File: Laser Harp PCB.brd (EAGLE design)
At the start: 78.7 x 76.3 mm, 35 parts, among them J1 DCJ0202, X1 22-23-2021, X10 22-23-2051, X11 22-23-2021, X12 22-23-2021, X2 22-23-2021, X3 22-23-2021, X4 22-23-2021, X5 22-23-2021, X6 22-23-2021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

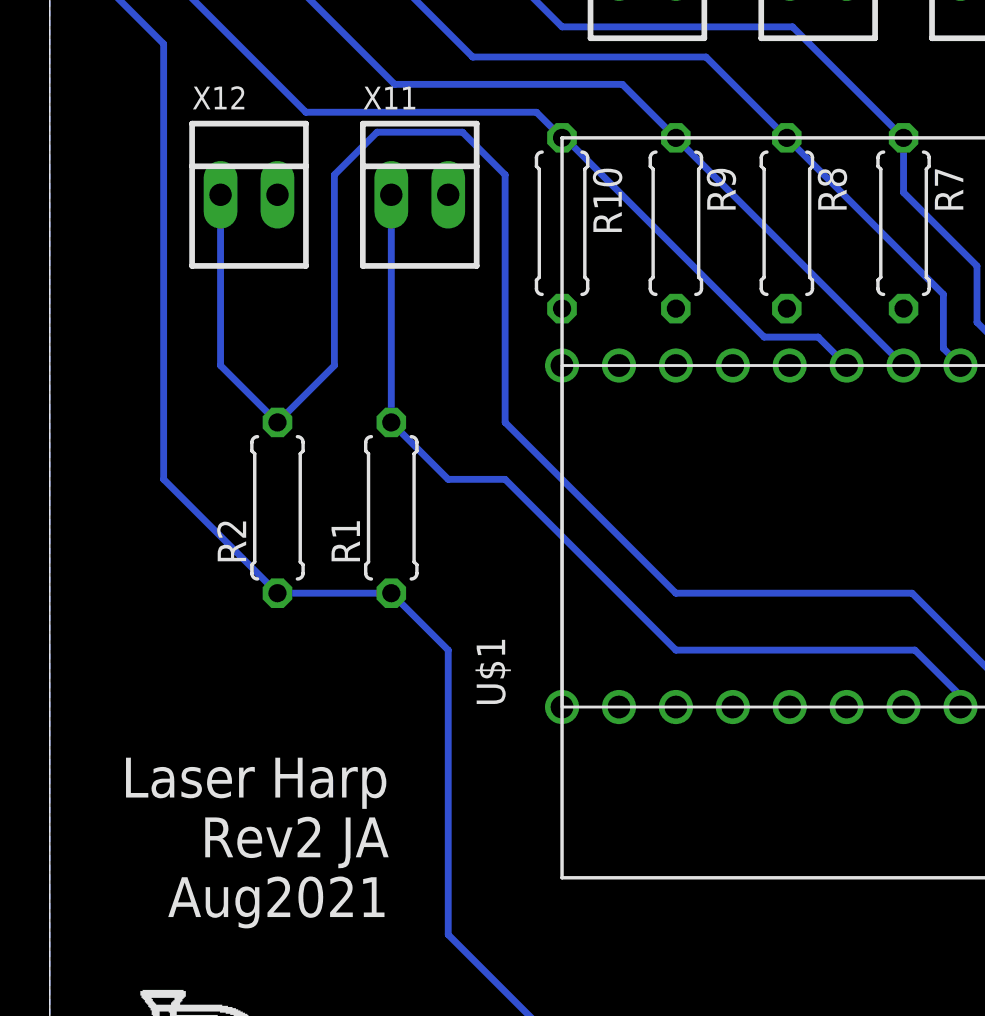
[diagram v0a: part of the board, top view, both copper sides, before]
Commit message: Update pin connections
The BJTs used to connect to pins 0 through 7 of the Teensy, but the Audio Shield uses pin 7 to transmit information from the micro sd card to the Teensy. I changed the connection from pin 7 to pin 8.
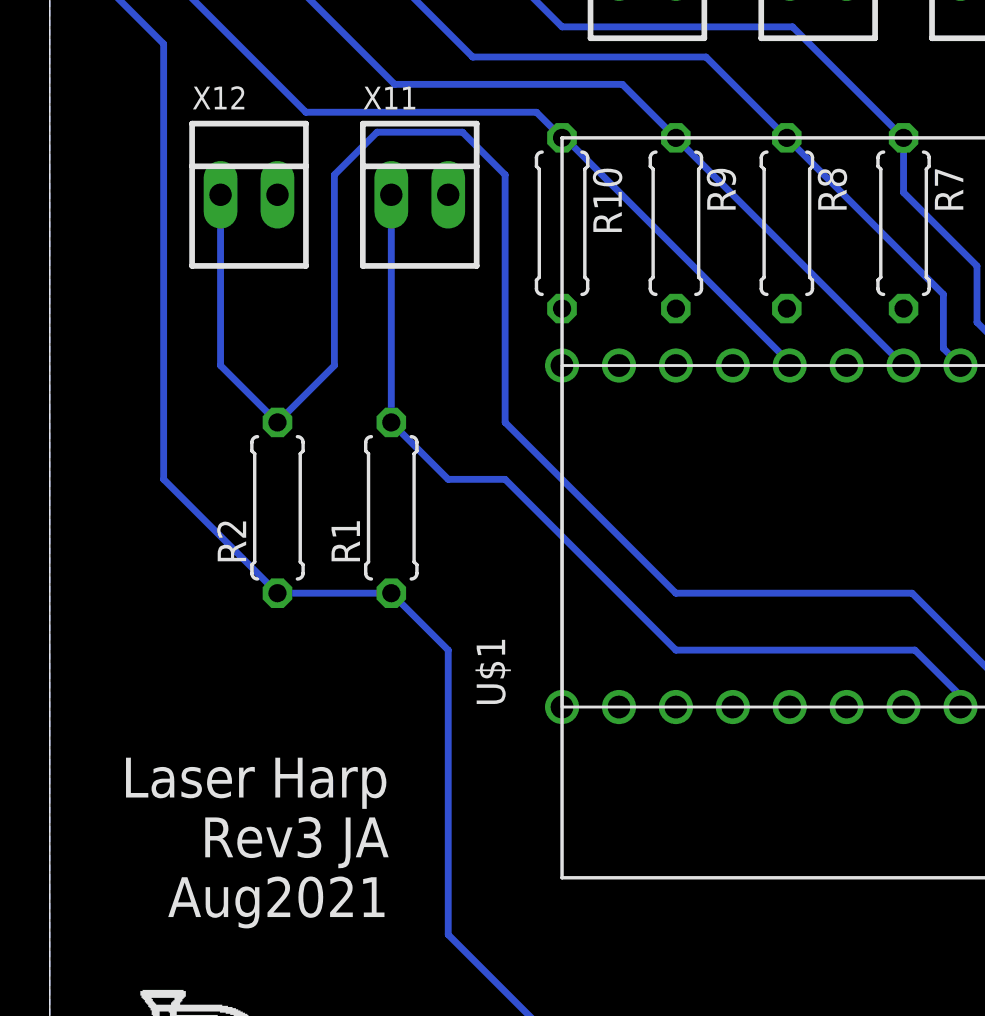
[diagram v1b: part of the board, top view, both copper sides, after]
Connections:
- net N$24: now also U$1.P$19; no longer U$1.P$20
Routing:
- net N$24: track 37.8 -> 35.3 mm
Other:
- board text added: "Laser Harp Rev3 JA Aug2021"
- board text removed: "Laser Harp Rev2 JA Aug2021"
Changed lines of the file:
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@@
 <wire x1="22.86" y1="50.8" x2="22.86" y2="17.78" width="0.1524" layer="21"/>
 <text x="15.1384" y="23.1394" size="1.778" layer="21" rot="R180">Laser Harp
-Rev2 JA
+Rev3 JA
 Aug2021</text>
 <rectangle x1="5.5626" y1="3.5306" x2="8.9662" y2="3.5814" layer="21"/>
@@
 </signal>
 <signal name="N$24">
-<contactref element="U$1" pad="P$20"/>
 <contactref element="T9" pad="E"/>
 <contactref element="R10" pad="1"/>
@@
 <wire x1="11.43" y1="51.943" x2="5.08" y2="58.293" width="0.3048" layer="16"/>
 <wire x1="21.717" y1="51.943" x2="11.43" y2="51.943" width="0.3048" layer="16"/>
-<wire x1="35.56" y1="40.64" x2="34.29" y2="41.91" width="0.3048" layer="16"/>
-<wire x1="31.877" y1="41.91" x2="22.987" y2="50.8" width="0.3048" layer="16"/>
-<wire x1="22.987" y1="50.8" x2="22.86" y2="50.8" width="0.3048" layer="16"/>
-<wire x1="34.29" y1="41.91" x2="31.877" y2="41.91" width="0.3048" layer="16"/>
+<wire x1="22.86" y1="50.8" x2="22.987" y2="50.8" width="0.3048" layer="16"/>
+<contactref element="U$1" pad="P$19"/>
+<wire x1="33.02" y1="40.767" x2="33.02" y2="40.64" width="0.3048" layer="16"/>
+<wire x1="22.987" y1="50.8" x2="33.02" y2="40.767" width="0.3048" layer="16"/>
 </signal>
 <signal name="N$27">
